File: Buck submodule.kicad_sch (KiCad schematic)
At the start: 6 parts, among them U1 TPL0102-100PWR, U3 TPS1H100BQPWPRQ1, U37 TPS1H100BQPWPRQ1, U38 INA4235AIYBJR, U4 TPS1H100BQPWPRQ1, U5 TPS1H100BQPWPRQ1

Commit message: HW-61 chore: FT4233 Wire'd up
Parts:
- removed U1: TPL0102-100PWR, semiconductor:TSSOP-14_P0.65_4.4x5x1.2, symbol integrated-circuit:TPL0102-100PWR
- removed U3, U37, U4, U5: TPS1H100BQPWPRQ1, semiconductor:HTSSOP-14-1EP_P0.65_4.4x5x1.2, symbol integrated-circuit:TPS1H100BQPWPRQ1
- added C1, C2: 10uF-1210_01, passive:Capacitor_1210, symbol capacitor:10uF-1210_01
- added C10, C7, C8, C9: 220nF-0402_02, passive:Capacitor_0402, symbol staging:220nF-0402_02
- added C11, C12, C13, C14: 22nF-0805_01, passive:Capacitor_0805, symbol capacitor:22nF-0805_01
- added C15, C16, C18, C19: 1uF-0402_01, passive:Capacitor_0402, symbol capacitor:1uF-0402_01
- added C17: 100nF-0402_01, passive:Capacitor_0402, symbol capacitor:100nF-0402_01
- added C3: 22pF-0402_01, passive:Capacitor_0402, symbol capacitor:22pF-0402_01
- added C4, C5, C6: 4.7uF-1206_02, passive:Capacitor_1206, symbol capacitor:4.7uF-1206_02
- added R1, R10, R11, R12, R13, R14, R15, R16, R17, R2, R4: 0R-0402_01, passive:Resistor_0402, symbol resistor:0R-0402_01
- added R3: 15.8k-0402_02, passive:Resistor_0402, symbol review:15.8k-0402_02
- added R5: 100k-0201_01, passive:Resistor_0201, symbol resistor:100k-0201_01
- added R6, R7, R8, R9: 1k-0402_01, passive:Resistor_0402, symbol resistor:1k-0402_01
- added U4: TPSM63610RDFR, review:B3QFN-22_P0.65_7.5x6.5x4, symbol staging:TPSM63610RDFR
- added U5, U6, U7, U8: TPS1HTC30AQPWPRQ1, semiconductor:HTSSOP-14-1EP_P0.65_4.4x5x1.2, symbol staging:TPS1HTC30AQPWPRQ1
- renumbered U38 to U9
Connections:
- net Current shunt/INPUT_CURRENT: now also C11.1, U5.10 (VOUT), U5.8 (VOUT), U5.9 (VOUT)
- net Current shunt1/INPUT_CURRENT: now also C12.1, U6.10 (VOUT), U6.8 (VOUT), U6.9 (VOUT)
- net Current shunt2/INPUT_CURRENT: now also C13.1, U7.10 (VOUT), U7.8 (VOUT), U7.9 (VOUT)
- net Current shunt3/INPUT_CURRENT: now also C14.1, U8.10 (VOUT), U8.8 (VOUT), U8.9 (VOUT)
- net PWR_SWITCH_EN_1: now also U5.2 (EN)
- net PWR_SWITCH_EN_2: now also U6.2 (EN)
- net PWR_SWITCH_EN_3: now also U7.2 (EN)
- net PWR_SWITCH_EN_4: now also U8.2 (EN)
- net +5V: now reaches U9.A4 (VS)
- net +5V: now also U9.B3 (EN), C17.1
- net GND: now reaches U9.B4 (GND)
- net GND: now also C1.2, C10.2, C11.2, C12.2, C13.2, C14.2, C17.2, C2.2, C4.2, C5.2, C6.2, C7.2, C8.2, C9.2, R1.2, R2.2, R3.1, R6.1, R7.1, R8.1, R9.1, U4.11 (AGND), U4.15 (MODE), U4.19 (PGND), U4.20 (PGND), U4.21 (AGND), U4.22 (AGND), U4.7 (AGND), U5.1 (GND), U5.15 (Thermal_Pad), U6.1 (GND), U6.15 (Thermal_Pad), U7.1 (GND), U7.15 (Thermal_Pad), U8.1 (GND), U8.15 (Thermal_Pad)
- net INA_A0: now reaches U9.C2 (A0)
- net INA_A1: now reaches U9.C3 (A1)
- net SCL: now reaches U9.C4 (SCL)
- net SDA: now reaches U9.D4 (SDA)
- net at U9.A1 (IN+2): now also R12.2
- net at U9.A2 (IN-1): now also R11.2
- net at U9.A3 (IN+1): now also R10.2
- net at U9.B1 (IN-2): now also R13.2
- net at U9.C1 (IN-3): now also R15.1
- net at U9.D1 (IN+3): now also R14.1
- net at U9.D2 (IN-4): now also R17.1
- net at U9.D3 (IN+4): now also R16.1
- new net: R9.2, U8.6 (SNS)
- new net: R2.1, U4.13 (PG)
- new net: R3.2, U4.12 (RT)
- new net: R1.1, U4.14 (SPSP)
- new net: R7.2, U6.6 (SNS)
- new net: R4.1, U4.2 (RBOOT)
- new net: R4.2, U4.3 (CBOOT)
- new net: R8.2, U7.6 (SNS)
- new net: R6.2, U5.6 (SNS)
- new net +24V: C1.1, C2.1, U4.1 (VIN1), U4.17 (EN), U4.18 (VIN2)
- new net +INA_BUCK_1: C15.1, R10.1
- new net +INA_BUCK_2: C16.1, R12.1
- new net +INA_BUCK_3: C18.1, R14.2
- new net +INA_BUCK_4: C19.1, R16.2
- new net -INA_BUCK_1: C15.2, R11.1
- new net -INA_BUCK_2: C16.2, R13.1
- new net -INA_BUCK_3: C18.2, R15.2
- new net -INA_BUCK_4: C19.2, R17.2
- new net 20V_BUCK_OUT: C10.1, C3.1, C4.1, C5.1, C6.1, C7.1, C8.1, C9.1, R5.2, U4.10 (VOUT2), U4.5 (VLDOIN), U4.9 (VOUT1), U5.12 (VS), U5.13 (VS), U5.14 (VS), U6.12 (VS), U6.13 (VS), U6.14 (VS), U7.12 (VS), U7.13 (VS), U7.14 (VS), U8.12 (VS), U8.13 (VS), U8.14 (VS)
- new net FB_RESISTOR_IN: C3.2, R5.1, U4.8 (FB)
- no-connect marks 0 -> 18
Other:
- note added: ""Connect to GND to disable spread spectrum""
- note added: ""If not used, PG can be left open or connected to GND""
- note added: ""These pins (AGND) must be connected to PGND""
- moved on the sheet: U9A, U9B

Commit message: Details to finish
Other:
- note added: "Buck regulator"
- note added: "Current sensing"
- note added: "Power switch and Current shunts"
- moved on the sheet: C1, C10, C11, C12, C13, C14, C15, C16, C17, C18, C19, C2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

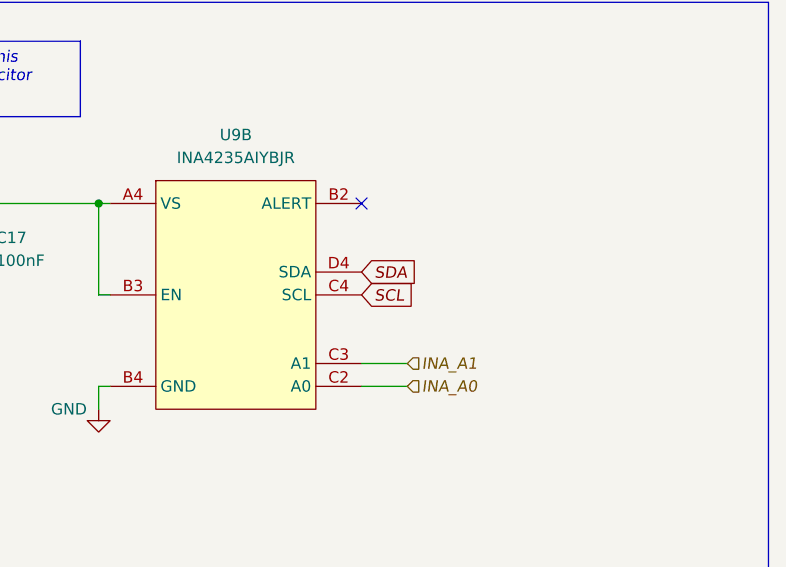
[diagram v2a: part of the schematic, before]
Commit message: HW-61/chore: Added simulation for switch ocntrol, organized the overall schematic, fixed the ERC errors. Still pending for the current sense components and negative side LDO control
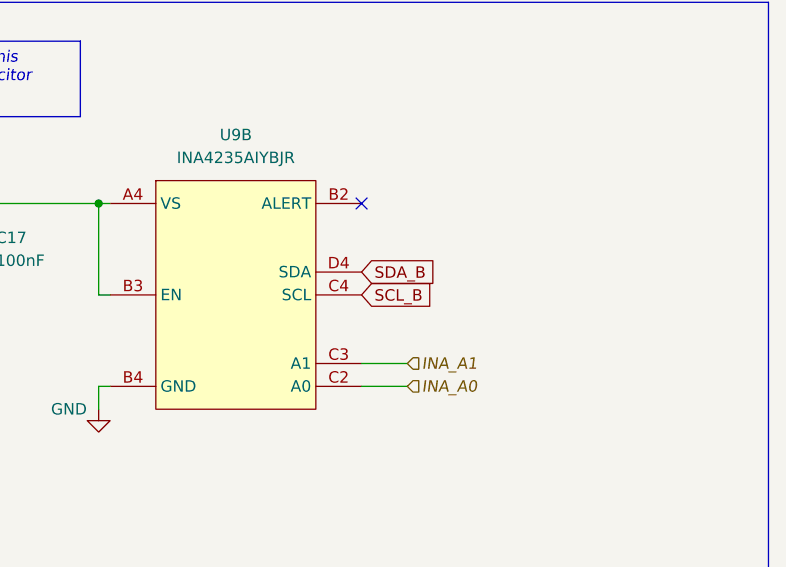
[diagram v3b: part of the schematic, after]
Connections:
- net SCL renamed SCL_B
- net SDA renamed SDA_B
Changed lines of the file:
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@@
 		)
 	)
-	(global_label "SDA"
+	(global_label "SCL_B"
 		(shape input)
-		(at 473.71 43.18 0)
+		(at 473.71 45.72 0)
 		(fields_autoplaced yes)
 		(effects
 			(font
 				(size 1.27 1.27)
-				(italic yes)
 			)
 			(justify left)
 		)
 		(property "Intersheetrefs" "${INTERSHEET_REFS}"
-			(at 480.2633 43.18 0)
+			(at 482.4404 45.72 0)
 			(effects
 				(font
@@
 		)
 	)
-	(global_label "SCL"
+	(global_label "SDA_B"
 		(shape input)
-		(at 473.71 45.72 0)
+		(at 473.71 43.18 0)
 		(fields_autoplaced yes)
 		(effects
 			(font
 				(size 1.27 1.27)
-				(italic yes)
 			)
 			(justify left)
 		)
 		(property "Intersheetrefs" "${INTERSHEET_REFS}"
-			(at 480.2028 45.72 0)
+			(at 482.5009 43.18 0)
 			(effects
 				(font
